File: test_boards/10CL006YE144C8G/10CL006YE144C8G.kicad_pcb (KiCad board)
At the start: 2 copper layers, 82 parts, among them IC1 10CL006YE144C8G, J1 CL_JTAG, U1 W25Q128JVS, Y1 SG-7050CAN

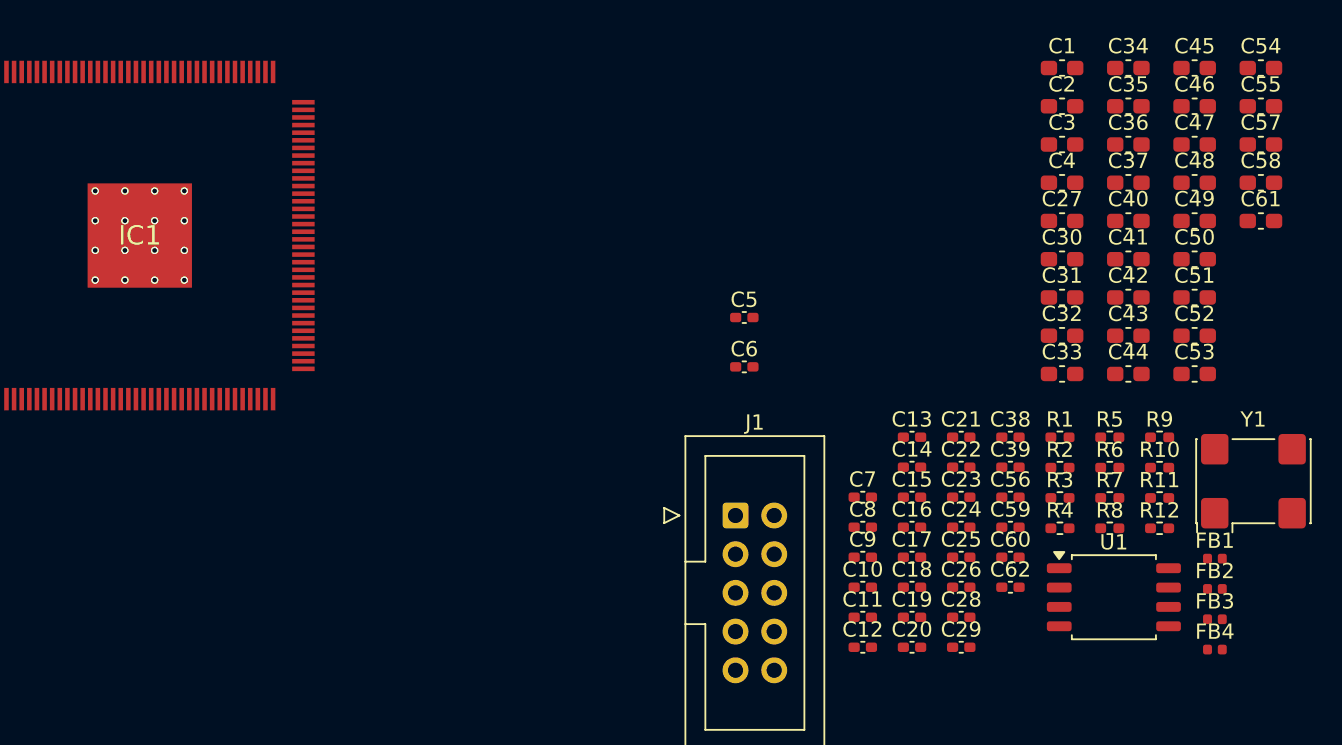
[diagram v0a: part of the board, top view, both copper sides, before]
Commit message: Добавлена проверка перекрытий
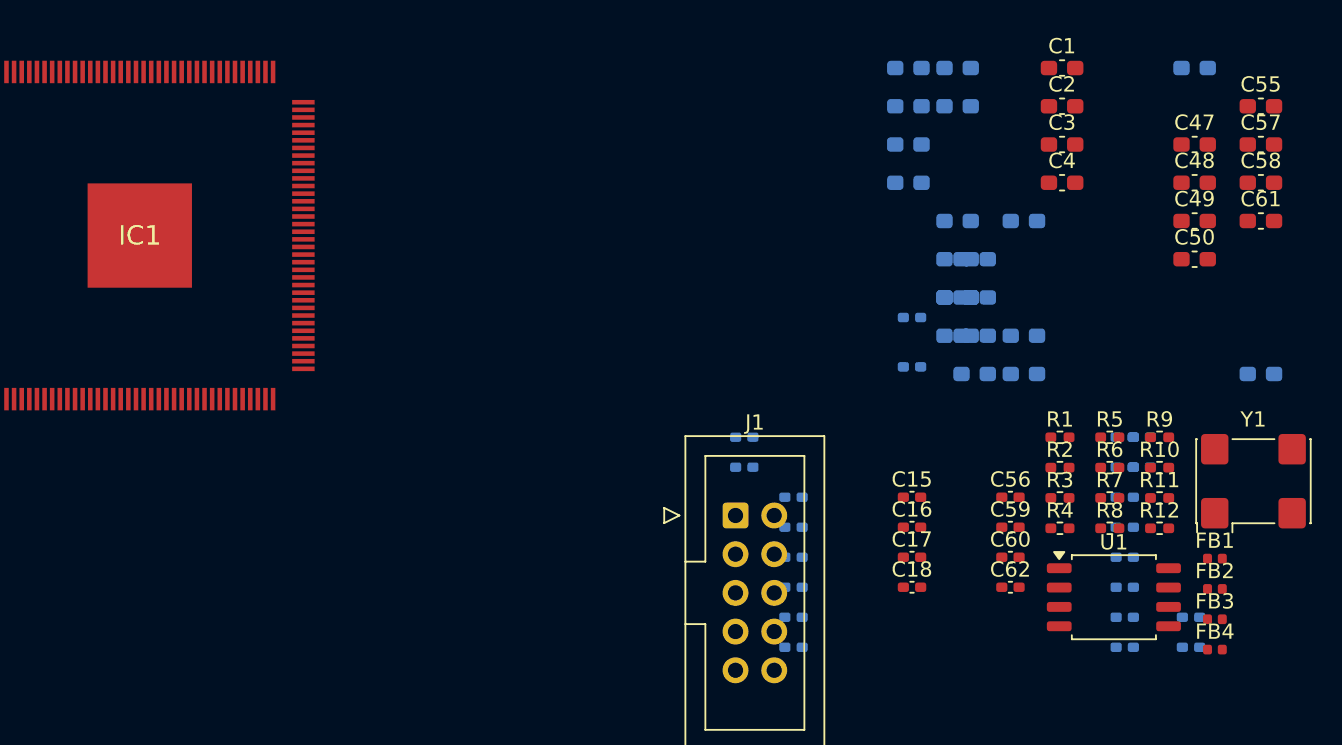
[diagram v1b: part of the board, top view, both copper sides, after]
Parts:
- C10, C11, C12, C13, C14, C19, C20, C21, C22, C23, C24, C25, C26, C27, C28, C29, C30, C31, C32, C33, C34, C35, C36, C37, C38, C39, C40, C41, C42, C43, C44, C45, C46, C5, C51, C52, C53, C54, C6, C7, C8, C9: moved to B.Cu
- moved C45 15.6 mm to (105.3, 60.0), turned to 180 degrees
- moved C46 15.6 mm to (105.3, 62.5), turned to 180 degrees
- moved C51 15.6 mm to (105.3, 75.1), turned to 180 degrees
- moved C52 15.6 mm to (105.3, 77.6), turned to 180 degrees
- moved C28 15.1 mm to (120.6, 96.0), turned to 180 degrees
- moved C29 15.1 mm to (120.6, 98.0), turned to 180 degrees
- moved C34 14.4 mm to (102.0, 60.0), turned to 180 degrees
- moved C35 14.4 mm to (102.0, 62.5), turned to 180 degrees
- moved C36 14.4 mm to (102.0, 65.0), turned to 180 degrees
- moved C37 14.4 mm to (102.0, 67.5), turned to 180 degrees
- moved C19 14.0 mm to (116.2, 96.0), turned to 180 degrees
- moved C20 14.0 mm to (116.2, 98.0), turned to 180 degrees
- moved C40 11.2 mm to (105.3, 70.0), turned to 180 degrees
- moved C41 11.2 mm to (105.3, 72.5), turned to 180 degrees
- moved C42 11.2 mm to (105.3, 75.1), turned to 180 degrees
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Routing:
- net GND: vias 16 -> 0

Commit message: Полная модернизация режима boundary
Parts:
- C10, C11, C12, C13, C14, C19, C20, C21, C22, C23, C24, C25, C26, C27, C28, C29, C30, C31, C32, C33, C34, C35, C36, C37, C38, C39, C40, C41, C42, C43, C44, C45, C46, C5, C51, C52, C53, C54, C6, C7, C8, C9: moved to F.Cu
- moved C45 15.6 mm to (120.8, 60.0), turned to 0 degrees
- moved C46 15.6 mm to (120.8, 62.5), turned to 0 degrees
- moved C51 15.6 mm to (120.8, 75.1), turned to 0 degrees
- moved C52 15.6 mm to (120.8, 77.6), turned to 0 degrees
- moved C28 15.1 mm to (105.5, 96.0), turned to 0 degrees
- moved C29 15.1 mm to (105.5, 98.0), turned to 0 degrees
- moved C34 14.4 mm to (116.5, 60.0), turned to 0 degrees
- moved C35 14.4 mm to (116.5, 62.5), turned to 0 degrees
- moved C36 14.4 mm to (116.5, 65.0), turned to 0 degrees
- moved C37 14.4 mm to (116.5, 67.5), turned to 0 degrees
- moved C19 14.0 mm to (102.3, 96.0), turned to 0 degrees
- moved C20 14.0 mm to (102.3, 98.0), turned to 0 degrees
- moved C40 11.2 mm to (116.5, 70.0), turned to 0 degrees
- moved C41 11.2 mm to (116.5, 72.5), turned to 0 degrees
- moved C42 11.2 mm to (116.5, 75.1), turned to 0 degrees
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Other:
- copper layers 2 -> 4

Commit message: Попытка рефакторинга
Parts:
- moved C5 67.8 mm to (153.4, 103.4)
- moved C6 67.3 mm to (153.4, 105.4)
- moved C10 57.7 mm to (153.4, 113.3)
- moved C11 57.7 mm to (153.4, 115.2)
- moved C12 57.7 mm to (153.4, 117.2)
- moved C21 57.7 mm to (159.9, 103.4)
- moved C22 57.7 mm to (159.9, 105.4)
- moved C25 57.7 mm to (159.9, 111.3)
- moved C26 57.7 mm to (159.9, 113.3)
- moved C28 57.7 mm to (159.9, 115.2)
- moved C29 57.7 mm to (159.9, 117.2)
- moved C36 57.7 mm to (170.9, 84.2)
- moved C38 57.7 mm to (163.1, 103.4)
- moved C39 57.7 mm to (163.1, 105.4)
- moved C40 57.7 mm to (170.9, 89.2)
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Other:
- copper layers 4 -> 2

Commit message: Добавлены диагностические скрипты
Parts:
- moved C1 7.67 mm to (159.5, 76.0), turned to 90 degrees
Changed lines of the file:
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@@
 	(footprint "Capacitor_SMD:C_0603_1608Metric_Pad1.08x0.95mm_HandSolder"
 		(layer "F.Cu")
-		(at 166.515 79.195)
+		(at 159.54 76 90)
 		(descr "Capacitor SMD 0603 (1608 Metric), square (rectangular) end terminal, IPC-7351 nominal with elongated pad for handsoldering. (Body size source: IPC-SM-782 page 76, https://www.pcb-3d.com/wordpress/wp-content/uploads/ipc-sm-782a_amendment_1_and_2.pdf)")
 		(tags "capacitor handsolder")
 		(property "Reference" "C1"
-			(at 0 -1.43 0)
+			(at 0 -1.43 90)
 			(layer "F.SilkS")
 			(effects
@@
 		)
 		(property "Value" "1uF"
-			(at 0 1.43 0)
+			(at 0 1.43 90)
 			(layer "F.Fab")
 			(effects
@@
 		)
 		(property "Datasheet" ""
-			(at 0 0 0)
+			(at 0 0 90)
 			(layer "F.Fab")
 			(hide yes)
@@
 		)
 		(property "Description" "Unpolarized capacitor"
-			(at 0 0 0)
+			(at 0 0 90)
 			(layer "F.Fab")
 			(hide yes)
@@
 		)
 		(fp_text user "${REFERENCE}"
-			(at 0 0 0)
+			(at 0 0 90)
 			(layer "F.Fab")
 			(effects
@@
 		)
 		(pad "1" smd roundrect
-			(at -0.8625 0)
+			(at -0.8625 0 90)
 			(size 1.075 0.95)
 			(layers "F.Cu" "F.Mask" "F.Paste")
@@
 		)
 		(pad "2" smd roundrect
-			(at 0.8625 0)
+			(at 0.8625 0 90)
 			(size 1.075 0.95)
 			(layers "F.Cu" "F.Mask" "F.Paste")
